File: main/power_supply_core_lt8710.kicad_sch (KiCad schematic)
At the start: 26 parts, among them Q601 Q_NMOS_GDS, Q602 Q_PMOS_GDS

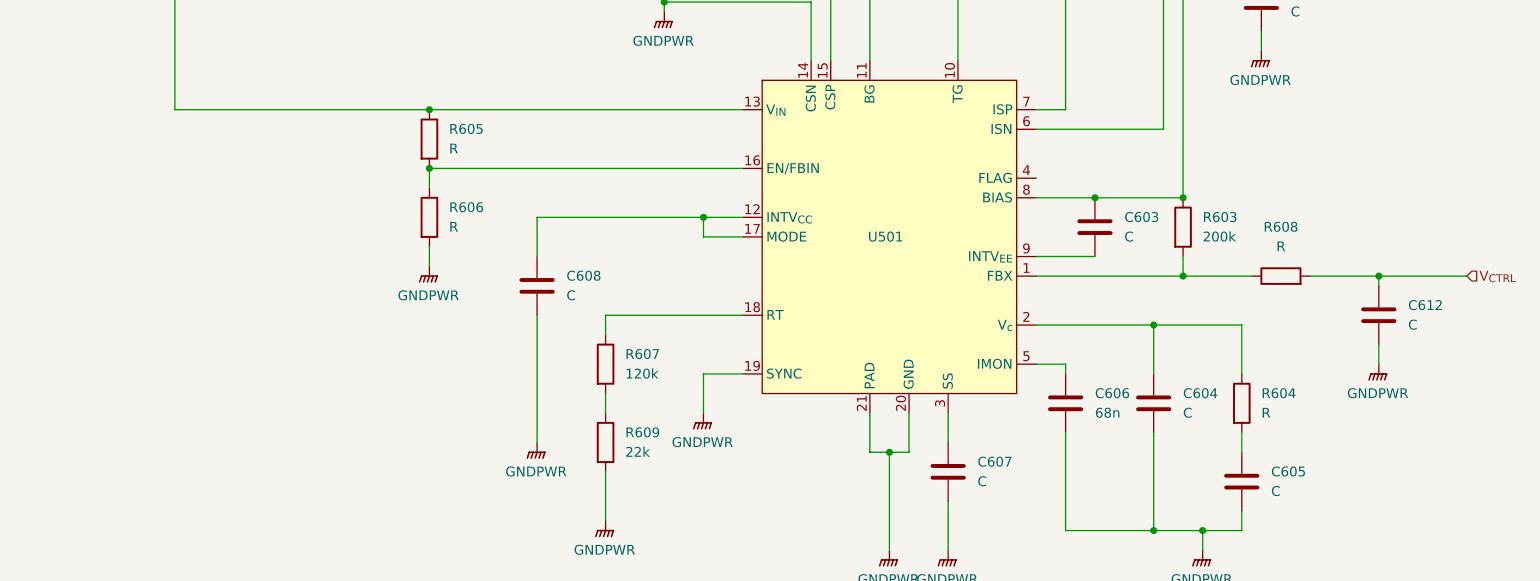
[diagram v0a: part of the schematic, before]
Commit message: Update components values
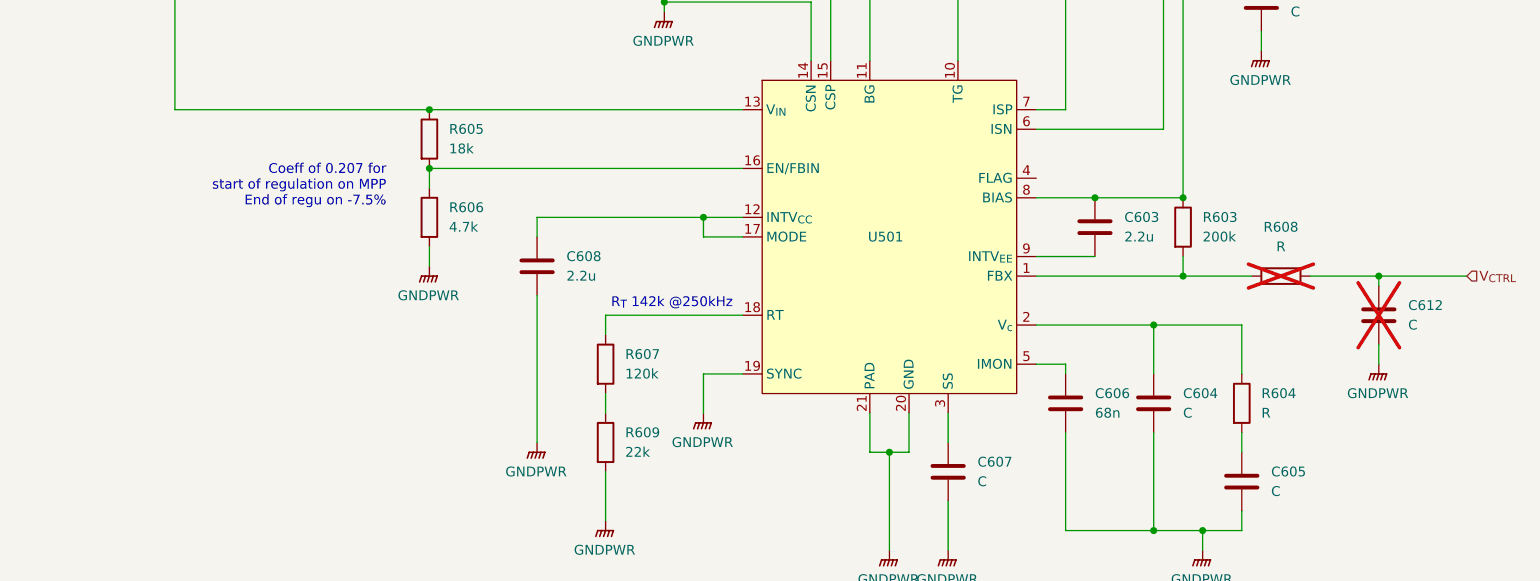
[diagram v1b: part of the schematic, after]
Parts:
- C603, C608: value C -> 2.2u
- C612, R608: now not fitted
- R605: value R -> 18k
- R606: value R -> 4.7k
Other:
- note added: "Coeff of 0.207 for start of regulation on MPP End of regu on -7.5%"
- note added: "R_{T} 142k @250kHz"
- moved on the sheet: C608
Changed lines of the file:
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@@
     (stroke (width 0) (type default))
   )
-  (wire (pts (xy 96.52 92.71) (xy 96.52 87.63))
+  (wire (pts (xy 96.52 90.17) (xy 96.52 87.63))
     (stroke (width 0) (type default))
   )
@@
     (stroke (width 0) (type default))
   )
-  (wire (pts (xy 96.52 100.33) (xy 96.52 116.84))
+  (wire (pts (xy 96.52 97.79) (xy 96.52 116.84))
     (stroke (width 0) (type default))
   )
@@
     )
   )
-  (image (at 57.15 93.98) (scale 0.557775)
+  (image (at 67.945 138.43) (scale 0.557775)
     (data
       iVBORw0KGgoAAAANSUhEUgAAA3kAAALvCAYAAADYuAw/AAAABHNCSVQICAgIfAhkiAAAABl0RVh0
@@
     )
   )
+  (text "R_{T} 142k @250kHz" (exclude_from_sim no)
+ (at 121.92 98.806 0)
+    (effects (font (size 1.27 1.27)) (justify right))
+  )
   (text "Input from 14 SunPower C60 (0.22m^{2})\n - 0.6V MPP 0.7V OC\n - 5.7A MPP 6.0A CC\n\nNominal 8.4V @ 5.7A (48W)\nIn France, will be 80% of rated current" (exclude_from_sim no)
     (at 19.685 26.035 0)
     (effects (font (size 1.27 1.27)) (justify left bottom))
   )
+  (text "Coeff of 0.207 for\nstart of regulation on MPP\nEnd of regu on -7.5%" (exclude_from_sim no)
+    (at 76.962 83.566 0)
+    (effects (font (size 1.27 1.27)) (justify right))
+  )
   (text "Target output is 20V\nMax used output is 16V\nTherefore, at most, 2.4A @ 20V\n\nUsing max cell current when caps discharged (6A)\n\nWe should handle 48W/6A/20V (not all same time)" (exclude_from_sim no)
     (at 232.664 29.464 0)
@@
   )
   (symbol (lib_id "Device:C") (at 205.74 100.33 0) (unit 1)
-    (exclude_from_sim no) (in_bom yes) (on_board yes) (dnp no) (fields_autoplaced)
+    (exclude_from_sim no) (in_bom yes) (on_board yes) (dnp yes) (fields_autoplaced)
     (property "Reference" "C612" (at 209.55 99.0599 0)
       (effects (font (size 1.27 1.27)) (justify left))
@@
       (effects (font (size 1.27 1.27)) (justify left))
     )
-    (property "Value" "R" (at 85.09 78.7399 0)
+    (property "Value" "18k" (at 85.09 78.7399 0)
       (effects (font (size 1.27 1.27)) (justify left))
     )
@@
   )
   (symbol (lib_id "Device:R") (at 193.04 95.25 90) (unit 1)
-    (exclude_from_sim no) (in_bom yes) (on_board yes) (dnp no) (fields_autoplaced)
+    (exclude_from_sim no) (in_bom yes) (on_board yes) (dnp yes) (fields_autoplaced)
     (property "Reference" "R608" (at 193.04 88.9 90)
       (effects (font (size 1.27 1.27)))
@@
     )
   )
-  (symbol (lib_id "Device:C") (at 96.52 96.52 0) (unit 1)
+  (symbol (lib_id "Device:C") (at 96.52 93.98 0) (unit 1)
     (exclude_from_sim no) (in_bom yes) (on_board yes) (dnp no) (fields_autoplaced)
-    (property "Reference" "C608" (at 100.33 95.2499 0)
+    (property "Reference" "C608" (at 100.33 92.7099 0)
       (effects (font (size 1.27 1.27)) (justify left))
     )
-    (property "Value" "C" (at 100.33 97.7899 0)
+    (property "Value" "2.2u" (at 100.33 95.2499 0)
       (effects (font (size 1.27 1.27)) (justify left))
     )
-    (property "Footprint" "" (at 97.4852 100.33 0)
+    (property "Footprint" "" (at 97.4852 97.79 0)
       (effects (font (size 1.27 1.27)) hide)
     )
-    (property "Datasheet" "~" (at 96.52 96.52 0)
+    (property "Datasheet" "~" (at 96.52 93.98 0)
       (effects (font (size 1.27 1.27)) hide)
     )
-    (property "Description" "Unpolarized capacitor" (at 96.52 96.52 0)
+    (property "Description" "Unpolarized capacitor" (at 96.52 93.98 0)
       (effects (font (size 1.27 1.27)) hide)
     )
@@
       (effects (font (size 1.27 1.27)) (justify left))
     )
-    (property "Value" "R" (at 85.09 88.8999 0)
+    (property "Value" "4.7k" (at 85.09 88.8999 0)
       (effects (font (size 1.27 1.27)) (justify left))
     )
@@
       (effects (font (size 1.27 1.27)) (justify left))
     )
-    (property "Value" "C" (at 172.72 90.1699 0)
+    (property "Value" "2.2u" (at 172.72 90.1699 0)
       (effects (font (size 1.27 1.27)) (justify left))
     )

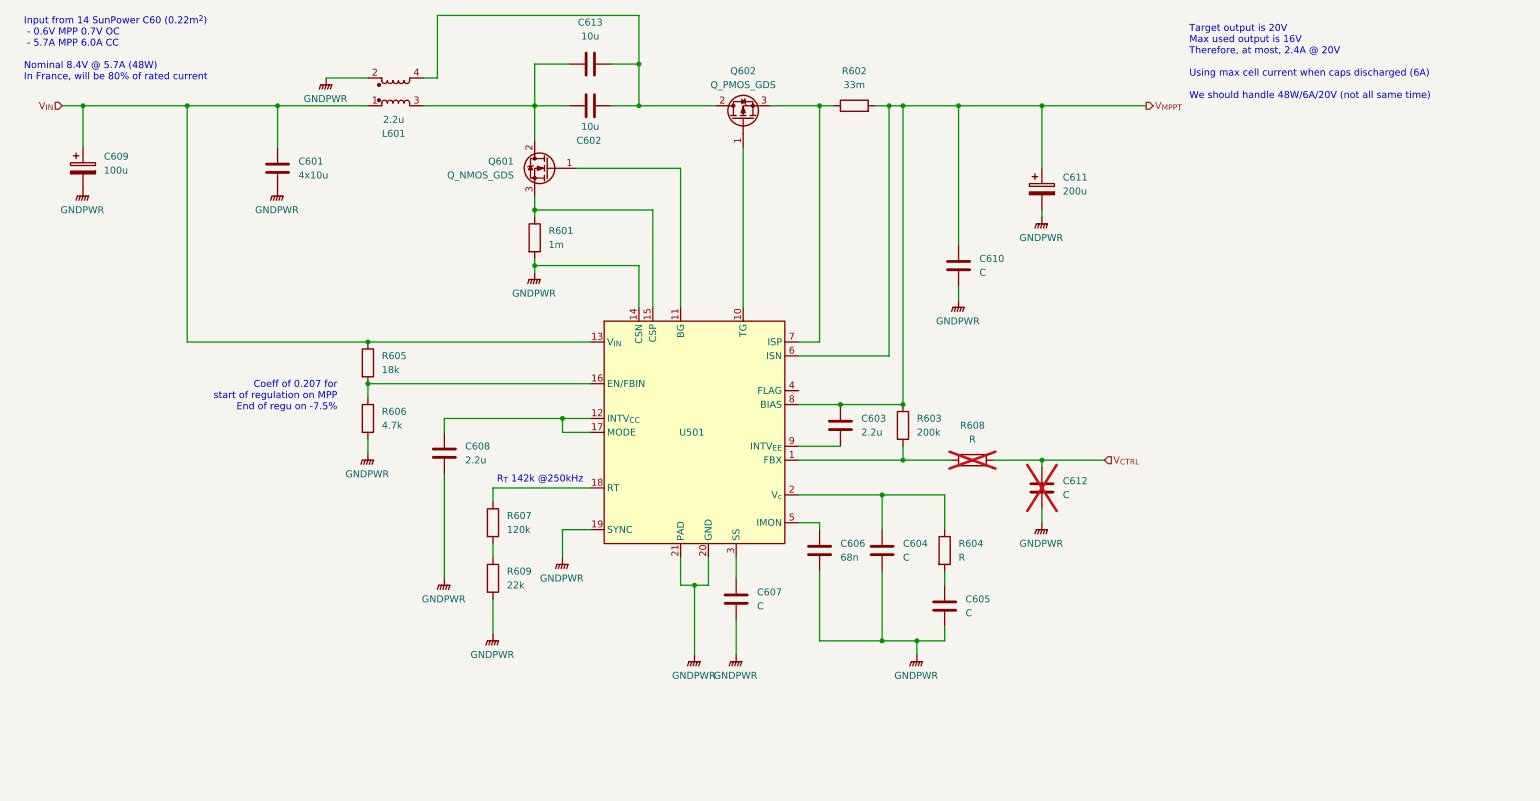
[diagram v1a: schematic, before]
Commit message: [PSU] Compute values for LT8710 PSU
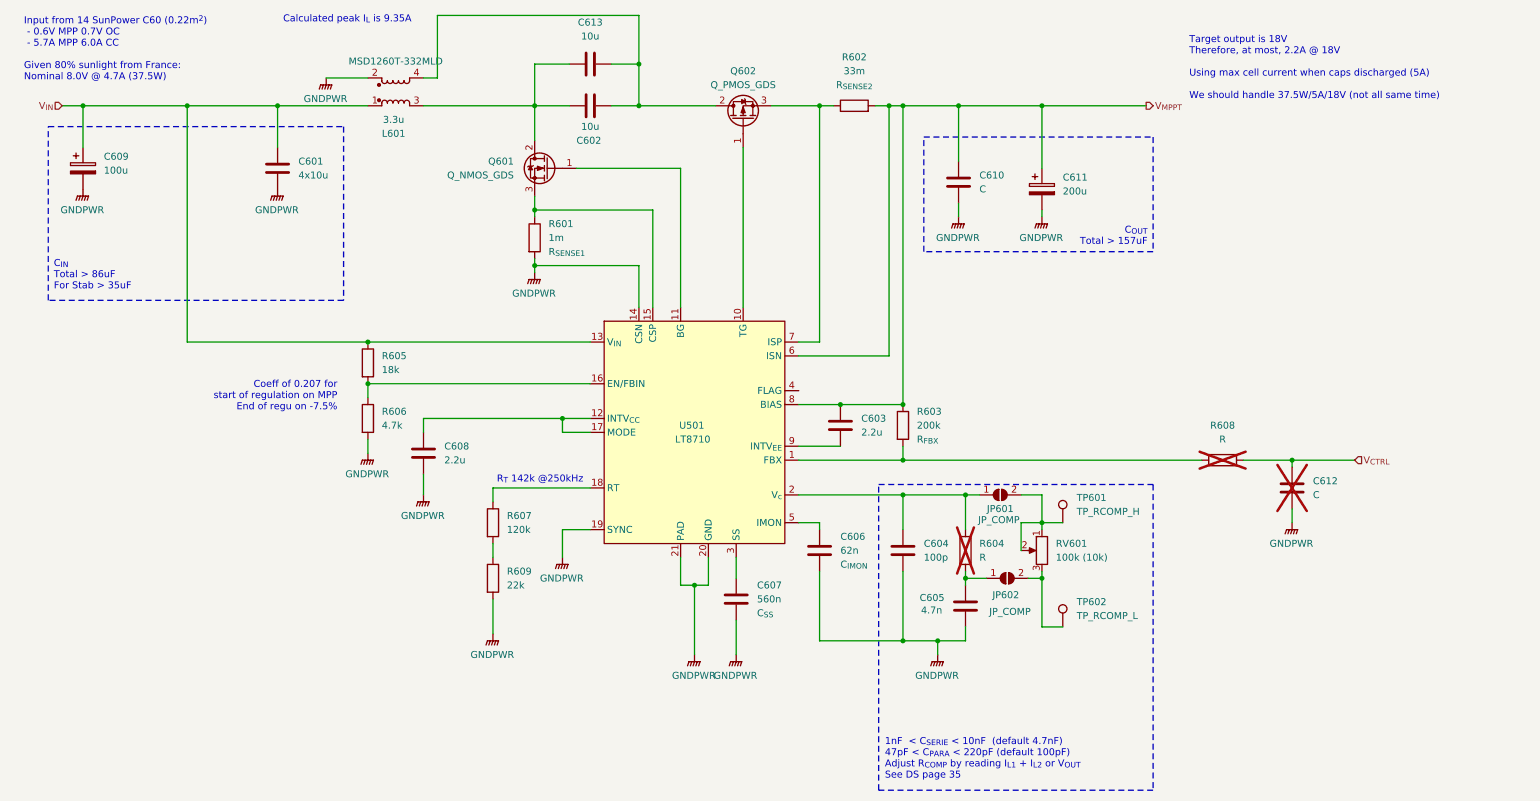
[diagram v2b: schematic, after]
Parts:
- added JP601, JP602: JP_COMP, symbol Jumper:SolderJumper_2_Open
- added RV601: 100k (10k), symbol Device:R_Potentiometer
- added TP601: TP_RCOMP_H, symbol Connector:TestPoint
- added TP602: TP_RCOMP_L, symbol Connector:TestPoint
- C604: value C -> 100p
- C605: value C -> 4.7n
- C606: value 68n -> 62n; Name (none) -> C_{IMON}
- C607: value C -> 560n; Name (none) -> C_{SS}
- L601: value 2.2u -> 3.3u; MPN (none) -> MSD1260T-332MLD
- R601: Name (none) -> R_{SENSE1}
- R602: Name (none) -> R_{SENSE2}
- R603: Name (none) -> R_{FBX}
- R604: now not fitted
- U501: value ~ -> LT8710
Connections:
- net at C604.1, R604.1, U501.2 (V_{c}): now also JP601.1 (A)
- net at C605.1, R604.2: now also JP602.1 (A)
- new net: JP601.2 (B), RV601.1, RV601.2, TP601.1
- new net: JP602.2 (B), RV601.3, TP602.1
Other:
- note added: "1nF < C_{SERIE} < 10nF (default 4.7nF) 47pF < C_{PARA} < 220pF (default 100pF) Adjust R_{COMP} by reading I_{L1} + I_{L2} or V_{OUT} See DS page 35"
- note added: "C_{IN} Total > 86uF For Stab > 35uF"
- note added: "C_{OUT} Total > 157uF"
- note added: "Calculated peak I_{L} is 9.35A"
- note added: "Input from 14 SunPower C60 (0.22m^{2}) - 0.6V MPP 0.7V OC - 5.7A MPP 6.0A CC Given 80% sunlight from France: Nominal 8.0V @ 4.7A (37.5W)"
- note added: "Target output is 18V Therefore, at most, 2.2A @ 18V Using max cell current when caps discharged (5A) We should handle 37.5W/5A/18V (not all same time)"
- note removed: "Input from 14 SunPower C60 (0.22m^{2}) - 0.6V MPP 0.7V OC - 5.7A MPP 6.0A CC Nominal 8.4V @ 5.7A (48W) In France, will be 80% of rated current"
- note removed: "Target output is 20V Max used output is 16V Therefore, at most, 2.4A @ 20V Using max cell current when caps discharged (6A) We should handle 48W/6A/20V (not all same time)"
- moved on the sheet: C604, C605, C608, C610, C612, R608

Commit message: PSU should be OK
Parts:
- removed Q601: Q_NMOS_GDS, symbol Device:Q_NMOS_GDS
- added Q602: TK4R3E06PL, Package_TO_SOT_THT:TO-220-3_Horizontal_TabUp, symbol Device:Q_NMOS_GDS
- JP601, JP602: symbol Jumper:SolderJumper_2_Open -> Jumper:SolderJumper_2_Bridged
- Q601: renamed from Q602; value Q_PMOS_GDS -> IXTP28P065T
- renumbered C613 to C601, C609 to C603, C601 to C604, C610 to C605, C611 to C606, C603 to C607, C612 to C609, C606 to C610, C604 to C611, C607 to C612, C605 to C613, R602 to R601, R601 to R602, R605 to R603, R606 to R604, R603 to R605, R608 to R606, R604 to R608, U501 to U601
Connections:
- net at C601.2, C602.2, L601.3: now also Q602.2 (D)
- net at R602.1, U601.15 (CSP): now also Q602.3 (S)
- net at U601.11 (BG): now also Q602.1 (G)
- net V_{MPPT} renamed V_{OUT}
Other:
- note added: "1nF < C_{SERIE} < 10nF (default 4.7nF) 47pF < C_{PARA} < 220pF (default 100pF) Adjust R_{COMP} by reading I_{L1} + I_{L2} or V_{OUT} Then solder fixed value and open bridges See DS page 35"
- note removed: "1nF < C_{SERIE} < 10nF (default 4.7nF) 47pF < C_{PARA} < 220pF (default 100pF) Adjust R_{COMP} by reading I_{L1} + I_{L2} or V_{OUT} See DS page 35"

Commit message: Progresses
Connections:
- net GNDPWR renamed PGND
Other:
- note added: "If required, solder R and C for external V_{OUT} control. Note that the external control can only *lower* the output voltage."
